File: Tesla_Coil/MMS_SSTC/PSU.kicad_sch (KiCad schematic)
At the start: 18 parts, among them J2 Screw_Terminal_01x02, SW1 SW_SPST, U4 LM7812_TO220, U5 LM7805_TO220

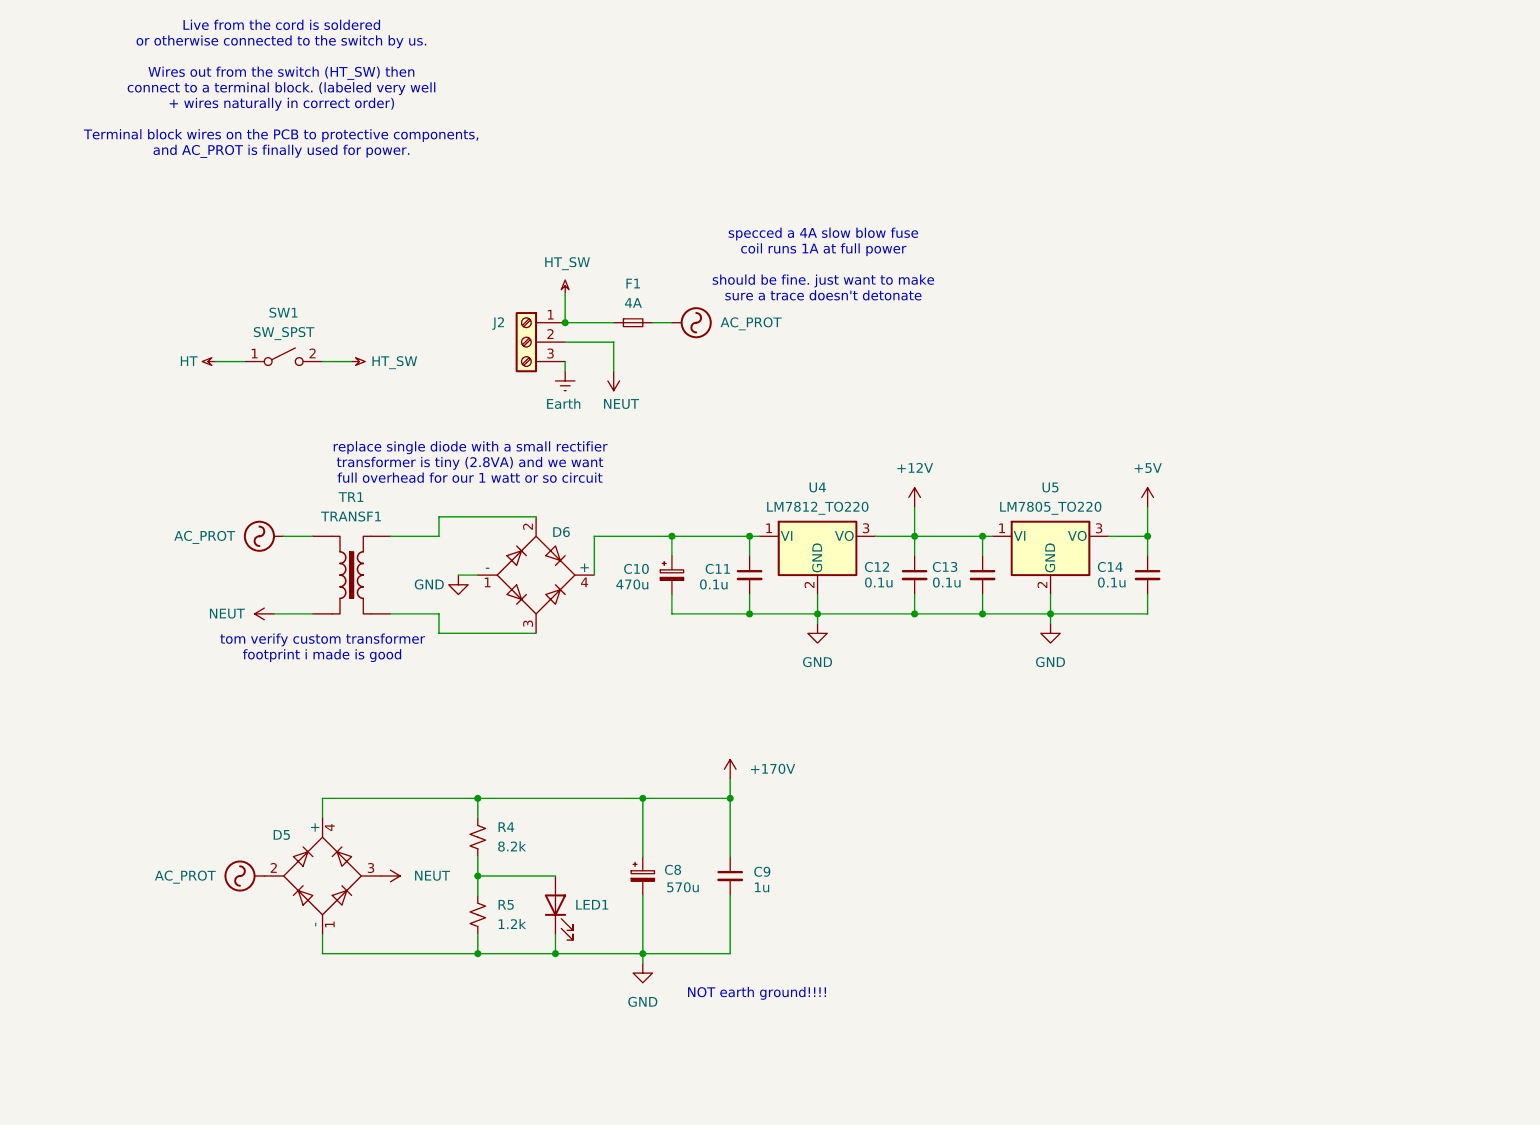
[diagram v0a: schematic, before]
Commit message: SSTC PCB finished
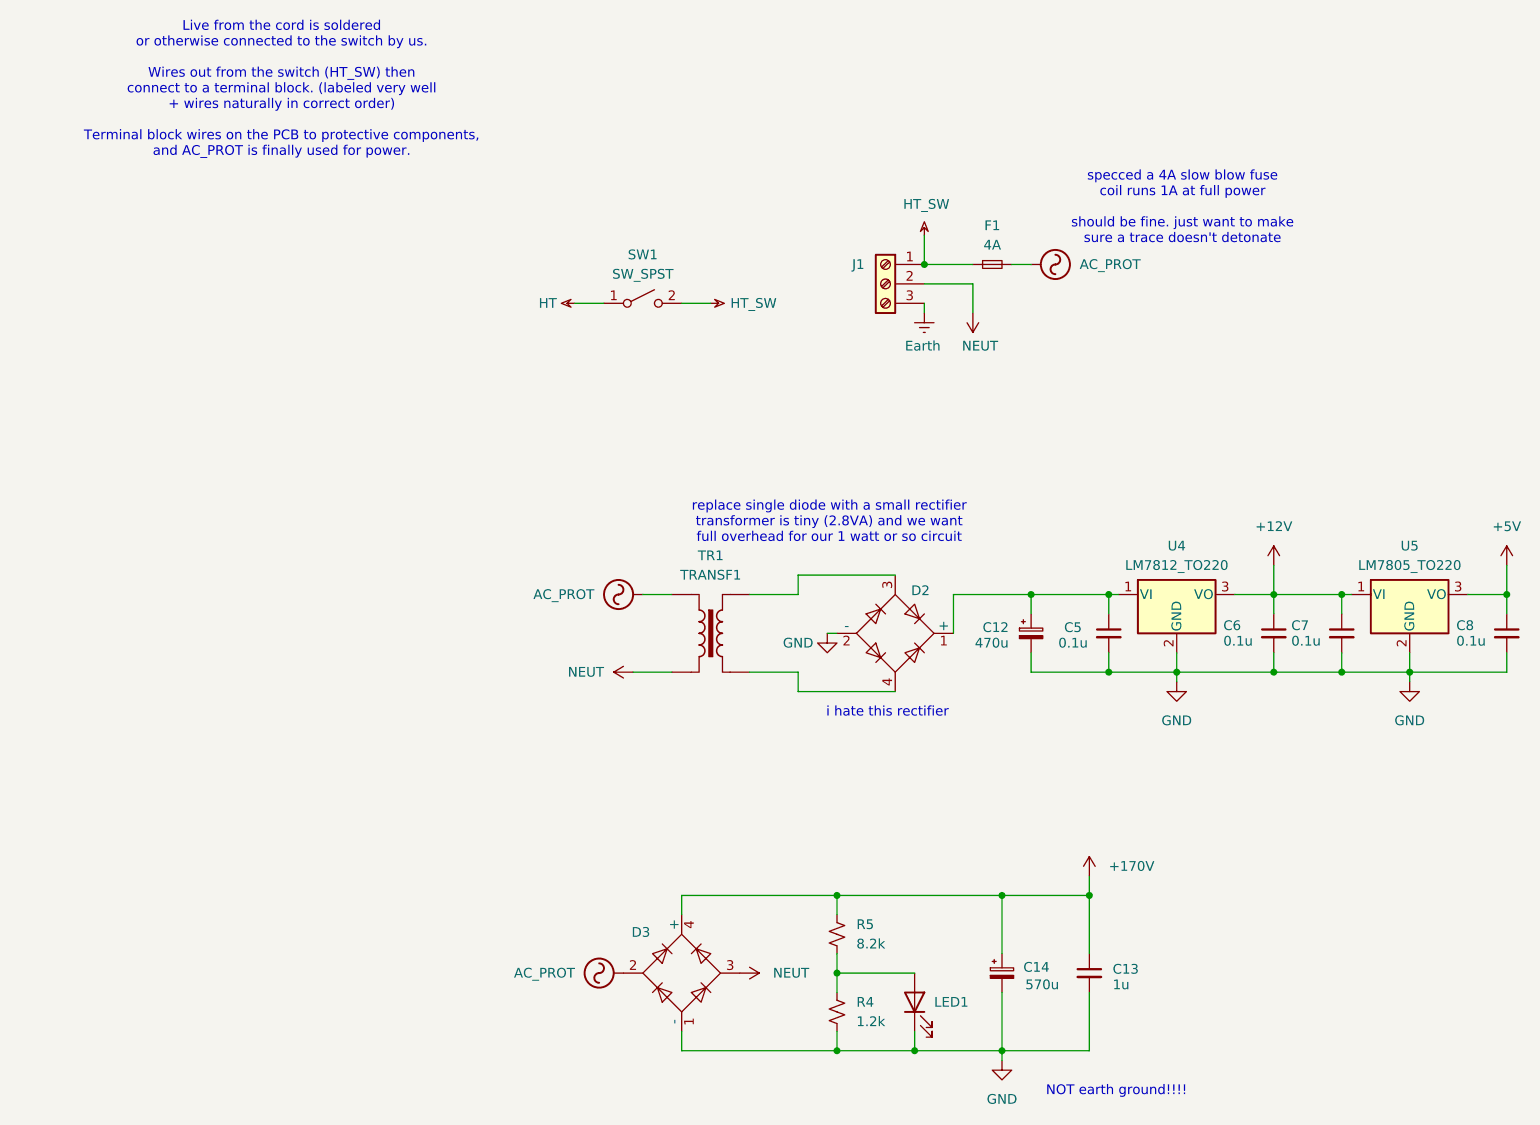
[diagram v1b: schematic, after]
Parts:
- D2: renamed from D6; symbol Diode_Bridge:B125C2300-1500A -> Diode_Bridge:B380C800DM
- D3: renamed from D5; footprint Diode_THT:Diode_Bridge_Vishay_GBU -> Diode_THT:Diode_Bridge_Vishay_GBL
- renumbered C10 to C12, C9 to C13, C8 to C14, C11 to C5, C12 to C6, C13 to C7, C14 to C8, J2 to J1, R5 to R4, R4 to R5
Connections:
- net GND: now also D2.2 (-); no longer D2.1 (-)
- net at C12.1, C5.1, U4.1 (VI): now also D2.1 (+); no longer D2.4 (+)
- net at TR1.3: now also D2.4; no longer D2.3
- net at TR1.4: now also D2.3; no longer D2.2
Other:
- note added: "i hate this rectifier"
- note removed: "tom verify custom transformer footprint i made is good"
- company: (none) -> Mines Maker Society
- title: (none) -> MMS SSTC
- moved on the sheet: C12, C13, C14, C5, C6, C7, C8, D2, D3, F1, J1, LED1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

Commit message: work on new case
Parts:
- C14: value 570u -> 1200u; DKPN 565-2951-ND -> 565-3692-ND
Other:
- note added: "C14 should be as large as possible, 1200u might even be low idfk"
- note added: "full bridge rectifiers are hell without isolation"
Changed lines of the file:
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@@
 		(comment 2 "Designed by William Layne")
+	)
+	(text "C14 should be as large as possible, \n1200u might even be low\nidfk\n"
+		(exclude_from_sim no)
+		(at 129.286 122.936 0)
+		(effects
+			(font
+				(size 1.27 1.27)
+			)
+		)
 	)
 	(text "NOT earth ground!!!!"
 		(exclude_from_sim no)
 		(at 153.416 155.194 0)
+		(effects
+			(font
+				(size 1.27 1.27)
+			)
+		)
+	)
+	(text "full bridge rectifiers are hell\nwithout isolation\n"
+		(exclude_from_sim no)
+		(at 88.138 154.432 0)
 		(effects
 			(font
@@
 			)
 		)
-		(property "Value" "570u"
+		(property "Value" "1200u"
 			(at 141.478 141.224 0)
 			(effects
@@
 			)
 		)
-		(property "DKPN" "565-2951-ND"
+		(property "DKPN" "565-3692-ND"
 			(at 138.43 139.7 0)
 			(effects

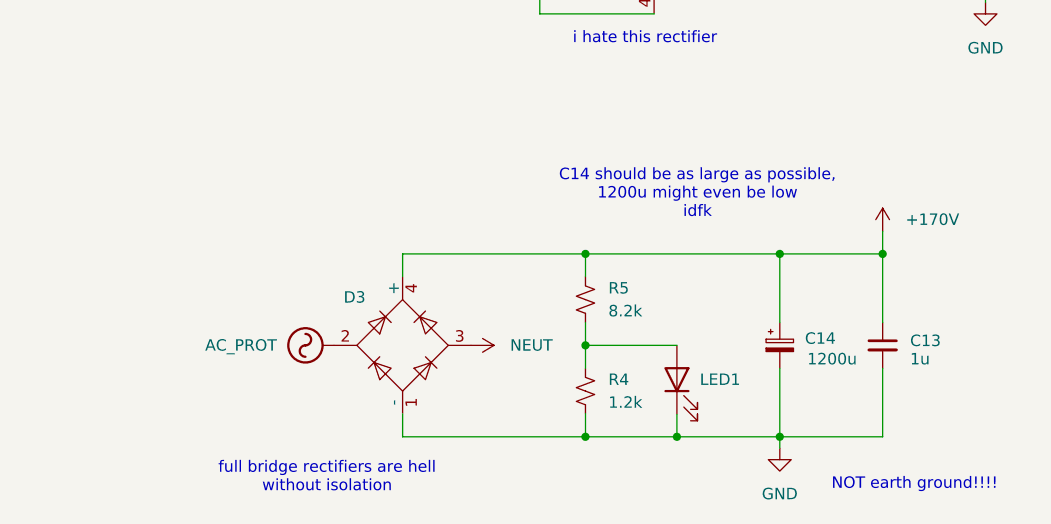
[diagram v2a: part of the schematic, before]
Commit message: finish acrylic case minus final tolerances
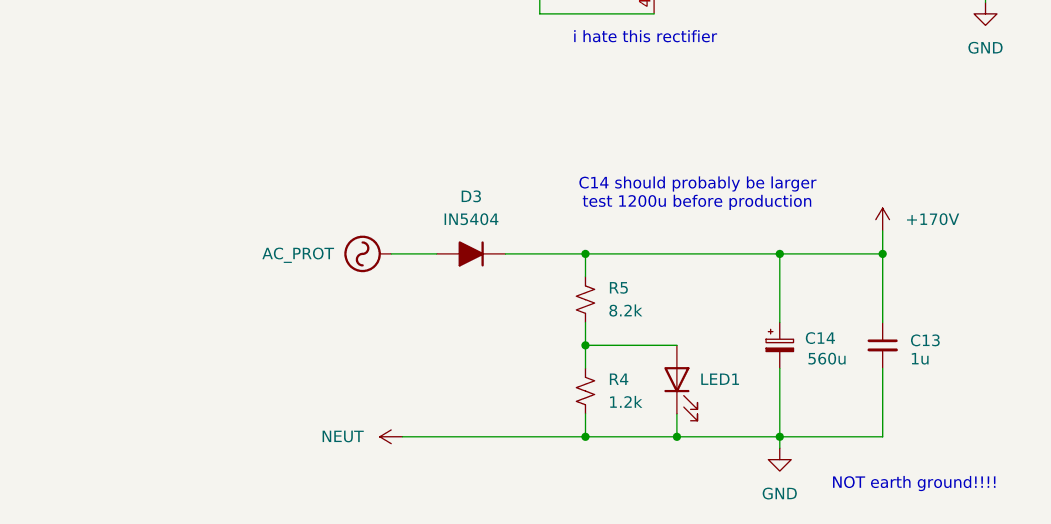
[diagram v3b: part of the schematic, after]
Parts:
- removed D3: B125C2300-1500A, Diode_THT:Diode_Bridge_Vishay_GBL, symbol Diode_Bridge:B125C2300-1500A
- added D3: IN5404, symbol Device:D_Filled
- C14: value 1200u -> 560u; DKPN 565-3692-ND -> 565-2951-ND
- SW1: DKPN 2057-SW-R3-1A-A-1-0-ND -> R4ABLKBLKFF0-ND
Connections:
- net NEUT is gone; now on net GND: J1.2 (Pin_2), TR1.2
- net +170V: now also D3.1 (K)
- net AC_PROT: now also D3.2 (A)
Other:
- note added: "C14 should probably be larger test 1200u before production"
- note removed: "C14 should be as large as possible, 1200u might even be low idfk"
- note removed: "full bridge rectifiers are hell without isolation"
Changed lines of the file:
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@@
 		(comment 2 "Designed by William Layne")
 	)
-	(text "C14 should be as large as possible, \n1200u might even be low\nidfk\n"
+	(text "C14 should probably be larger\ntest 1200u before production\n"
 		(exclude_from_sim no)
 		(at 129.286 122.936 0)
@@
 		)
 	)
-	(text "full bridge rectifiers are hell\nwithout isolation\n"
-		(exclude_from_sim no)
-		(at 88.138 154.432 0)
-		(effects
-			(font
-				(size 1.27 1.27)
-			)
-		)
-	)
 	(text "i hate this rectifier"
 		(exclude_from_sim no)
@@
 	)
 	(junction
-		(at 116.84 129.54)
-		(diameter 0)
-		(color 0 0 0 0)
-	)
-	(junction
 		(at 142.24 90.17)
 		(diameter 0)
@@
 	)
 	(junction
+		(at 116.84 129.54)
+		(diameter 0)
+		(color 0 0 0 0)
+	)
+	(junction
 		(at 152.4 90.17)
 		(diameter 0)
@@
 	(wire
 		(pts
-			(xy 96.52 149.86) (xy 96.52 147.32)
-		)
-		(stroke
-			(width 0)
-			(type default)
-		)
-	)
-	(wire
-		(pts
 			(xy 132.08 90.17) (xy 142.24 90.17)
 		)
@@
 	(wire
 		(pts
-			(xy 96.52 129.54) (xy 116.84 129.54)
-		)
-		(stroke
-			(width 0)
-			(type default)
-		)
-	)
-	(wire
-		(pts
 			(xy 142.24 97.79) (xy 142.24 100.33)
 		)
@@
 	(wire
 		(pts
+			(xy 95.25 129.54) (xy 100.33 129.54)
+		)
+		(stroke
+			(width 0)
+			(type default)
+		)
+	)
+	(wire
+		(pts
 			(xy 96.52 52.07) (xy 100.33 52.07)
 		)
@@
 	(wire
 		(pts
+			(xy 107.95 129.54) (xy 116.84 129.54)
+		)
+		(stroke
+			(width 0)
+			(type default)
+		)
+	)
+	(wire
+		(pts
 			(xy 139.7 46.99) (xy 142.24 46.99)
 		)
@@
 		(pts
 			(xy 128.27 52.07) (xy 128.27 53.34)
-		)
-		(stroke
-			(width 0)
-			(type default)
-		)
-	)
-	(wire
-		(pts
-			(xy 96.52 129.54) (xy 96.52 132.08)
 		)
 		(stroke
@@
 			)
 		)
-		(property "Value" "1200u"
+		(property "Value" "560u"
 			(at 141.478 141.224 0)
 			(effects
@@
 			)
 		)
-		(property "DKPN" "565-3692-ND"
+		(property "DKPN" "565-2951-ND"
 			(at 138.43 139.7 0)
 			(effects
@@
 				(path "/b29a3901-c128-4c19-b69f-61de71283b43/bfaa6adf-6b83-46d0-b8b3-f415df3d6008"
 					(reference "C14")
+					(unit 1)
+				)
+			)
+		)
+	)
+	(symbol
+		(lib_id "Device:D_Filled")
+		(at 104.14 129.54 180)
+		(unit 1)
+		(exclude_from_sim no)
+		(in_bom yes)
+		(on_board yes)
+		(dnp no)
+		(fields_autoplaced yes)
+		(property "Reference" "D3"
+			(at 104.14 123.19 0)
+			(effects
+				(font
+					(size 1.27 1.27)
+				)
+			)
+		)
+		(property "Value" "IN5404"
+			(at 104.14 125.73 0)
+			(effects
+				(font
+					(size 1.27 1.27)
+				)
+			)
+		)
+		(property "Footprint" ""
+			(at 104.14 129.54 0)
+			(effects
+				(font
+					(size 1.27 1.27)
+				)
+				(hide yes)
+			)
+		)
+		(property "Datasheet" "~"
+			(at 104.14 129.54 0)
+			(effects
+				(font
+					(size 1.27 1.27)
+				)
+				(hide yes)
+			)
+		)
+		(property "Description" "Diode, filled shape"
+			(at 104.14 129.54 0)
+			(effects
+				(font
+					(size 1.27 1.27)
+				)
+				(hide yes)
+			)
+		)
+		(property "Sim.Device" "D"
+			(at 104.14 129.54 0)
+			(effects
+				(font
+					(size 1.27 1.27)
+				)
+				(hide yes)
+			)
+		)
+		(property "Sim.Pins" "1=K 2=A"
+			(at 104.14 129.54 0)
+			(effects
+				(font
+					(size 1.27 1.27)
+				)
+				(hide yes)
+			)
+		)
+		(pin "2"
+		)
+		(pin "1"
+		)
+		(instances
+			(project ""
+				(path "/b29a3901-c128-4c19-b69f-61de71283b43/bfaa6adf-6b83-46d0-b8b3-f415df3d6008"
+					(reference "D3")
 					(unit 1)
 				)
@@
 			)
 		)
-		(property "DKPN" "2057-SW-R3-1A-A-1-0-ND"
+		(property "DKPN" "R4ABLKBLKFF0-ND"
 			(at 91.44 52.07 0)
 			(effects
@@
 	)
 	(symbol
-		(lib_id "Diode_Bridge:B125C2300-1500A")
-		(at 96.52 139.7 90)
-		(unit 1)
-		(exclude_from_sim no)
-		(in_bom yes)
-		(on_board yes)
-		(dnp no)
-		(property "Reference" "D3"
-			(at 91.186 134.366 90)
-			(effects
-				(font
-					(size 1.27 1.27)
-				)
-			)
-		)
-		(property "Value" "B125C2300-1500A"
-			(at 81.534 135.89 90)
-			(effects
-				(font
-					(size 1.27 1.27)
-				)
-				(hide yes)
-			)
-		)
-		(property "Footprint" "Diode_THT:Diode_Bridge_Vishay_GBL"
-			(at 93.345 135.89 0)
-			(effects
-				(font
-					(size 1.27 1.27)
-				)
-				(justify left)
-				(hide yes)
-			)
-		)
-		(property "Datasheet" ""
-			(at 96.52 139.7 0)
-			(effects
-				(font
-					(size 1.27 1.27)
-				)
-				(hide yes)
-			)
-		)
-		(property "Description" "Silicon Bridge Rectifier, 125V Vrms, 1.5A If, pins=-AA+, SIL-package"
-			(at 96.52 139.7 0)
-			(effects
-				(font
-					(size 1.27 1.27)
-				)
-				(hide yes)
-			)
-		)
-		(property "DKPN" "GBU810DI-ND"
-			(at 96.52 139.7 0)
-			(effects
-				(font
-					(size 1.27 1.27)
-				)
-				(hide yes)
-			)
-		)
-		(pin "3"
-		)
-		(pin "4"
-		)
-		(pin "2"
-		)
-		(pin "1"
-		)
-		(instances
-			(project "MMS_SSTC"
-				(path "/b29a3901-c128-4c19-b69f-61de71283b43/bfaa6adf-6b83-46d0-b8b3-f415df3d6008"
-					(reference "D3")
-					(unit 1)
-				)
-			)
-		)
-	)
-	(symbol
 		(lib_id "power:NEUT")
 		(at 134.62 53.34 180)
@@
 	(symbol
 		(lib_id "power:AC")
-		(at 88.9 139.7 90)
+		(at 95.25 129.54 90)
 		(unit 1)
 		(exclude_from_sim no)
@@
 		(fields_autoplaced yes)
 		(property "Reference" "#PWR018"
-			(at 91.44 139.7 0)
+			(at 97.79 129.54 0)
 			(effects
 				(font
@@
 		)
 		(property "Value" "AC_PROT"
-			(at 82.55 139.6999 90)
+			(at 88.9 129.5399 90)
 			(effects
 				(font
@@
 		)
 		(property "Footprint" ""
-			(at 88.9 139.7 0)
+			(at 95.25 129.54 0)
 			(effects
 				(font
@@
 		)
 		(property "Datasheet" ""
-			(at 88.9 139.7 0)
+			(at 95.25 129.54 0)
 			(effects
 				(font
@@
 		)
 		(property "Description" "Power symbol creates a global label with name \"AC\""
-			(at 88.9 139.7 0)
+			(at 95.25 129.54 0)
 			(effects
 				(font
@@
 	(symbol
 		(lib_id "power:NEUT")
-		(at 104.14 139.7 270)
+		(at 96.52 149.86 90)
 		(unit 1)
 		(exclude_from_sim no)
@@
 		(dnp no)
 		(property "Reference" "#PWR021"
-			(at 100.33 139.7 0)
+			(at 100.33 149.86 0)
 			(effects
 				(font
@@
 		)
 		(property "Value" "NEUT"
-			(at 108.458 139.7 90)
+			(at 92.202 149.86 90)
 			(effects
 				(font
@@
 		)
 		(property "Footprint" ""
-			(at 104.14 139.7 0)
+			(at 96.52 149.86 0)
 			(effects
 				(font
@@
 		)
 		(property "Datasheet" ""
-			(at 104.14 139.7 0)
+			(at 96.52 149.86 0)
 			(effects
 				(font
@@
 		)
 		(property "Description" "Power symbol creates a global label with name \"NEUT\""
-			(at 104.14 139.7 0)
-			(effects
-				(font
+			(at 96.52 149.86 0)
+			(effects
+				(font
